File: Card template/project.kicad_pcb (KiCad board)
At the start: 2 copper layers, 51.5 x 22 mm, 3 parts, among them U1 24LC32, X0 Card Edge

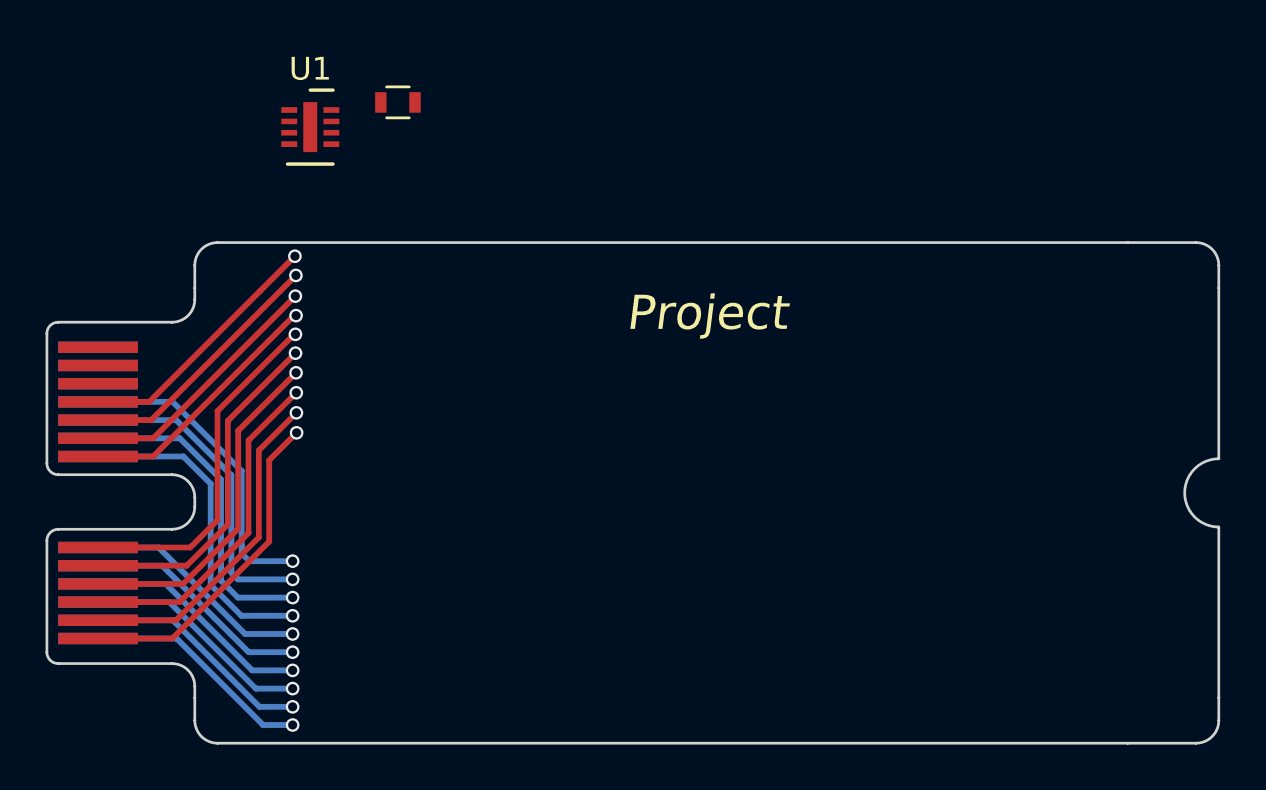
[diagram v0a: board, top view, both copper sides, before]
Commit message: EEPROM footprint update
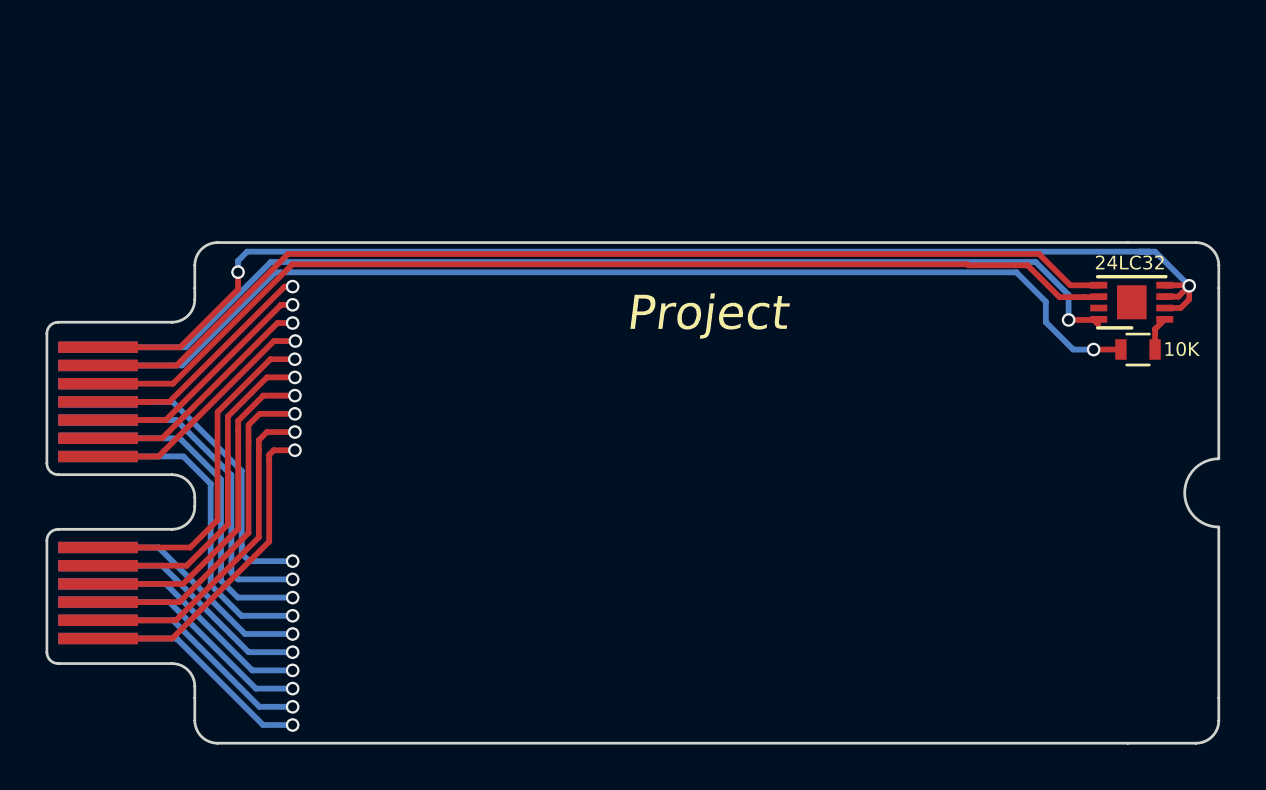
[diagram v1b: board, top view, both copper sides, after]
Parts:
- U1: footprint Package_DFN_QFN:DFN-8-1EP_2x3mm_P0.5mm_EP0.61x2.2mm -> footprints:DFN-8-1EP_3x2mm
- moved U1 36.9 mm to (47.7, -18.5), turned to 180 degrees
- moved R1 34.3 mm to (48.0, -16.4), turned to 180 degrees
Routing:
- net GND: track 0.00 -> 55.8 mm, vias 0 -> 2
- net /A: track 0.00 -> 48.6 mm, vias 0 -> 1
- net +5V: track 0.00 -> 47.3 mm, vias 0 -> 1
- net /D3_SCL: track 0.00 -> 46.9 mm
- net /D2_SDA: track 0.00 -> 46.6 mm
- net /19: track 11.3 -> 13.0 mm
- net /20: track 11.3 -> 12.9 mm
- net Net-(R1-Pad1): track 0.00 -> 1.50 mm
- net /18: track 11.3 -> 10.6 mm
- net /16: track 15.4 -> 14.9 mm

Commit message: Updates
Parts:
- moved U1 2.68 mm to (45.0, -18.5)
- moved R1 2.10 mm to (48.0, -18.5), turned to 90 degrees
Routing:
- net GND: track 55.8 -> 49.2 mm, vias 2 -> 0
- net /A: track 48.6 -> 53.7 mm
- net /19: track 13.0 -> 16.0 mm
- net /D3_SCL: track 46.9 -> 44.3 mm
- net /D2_SDA: track 46.6 -> 44.1 mm
- net +5V: track 47.3 -> 46.3 mm
- net /13: track 14.9 -> 14.0 mm
- net /12: track 14.6 -> 13.9 mm
- net /15: track 14.9 -> 14.2 mm
- net /14: track 14.9 -> 14.2 mm
- net /11: track 14.5 -> 13.9 mm
